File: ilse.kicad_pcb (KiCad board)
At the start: 2 copper layers, 80.9 x 128.5 mm, 89 parts, among them J1 OUT, J2 EURO RACK POWER, J3 CV Inputs, J4 1V/Oct, J5 Gate, J6 Cutoff, J7 Filter In, Q1 BC560, Q2 BC560, Q3 BC560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

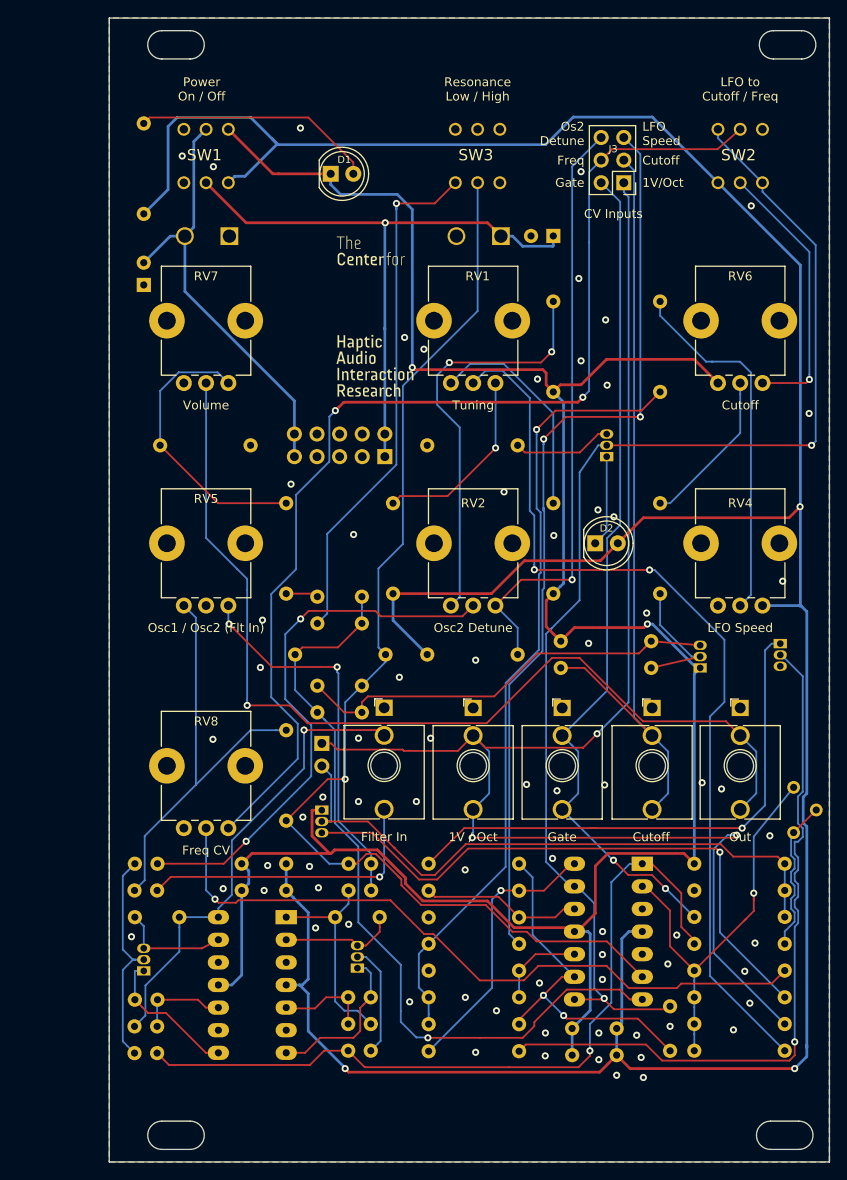
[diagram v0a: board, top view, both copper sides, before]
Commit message: removed power switch, added power protection diodes
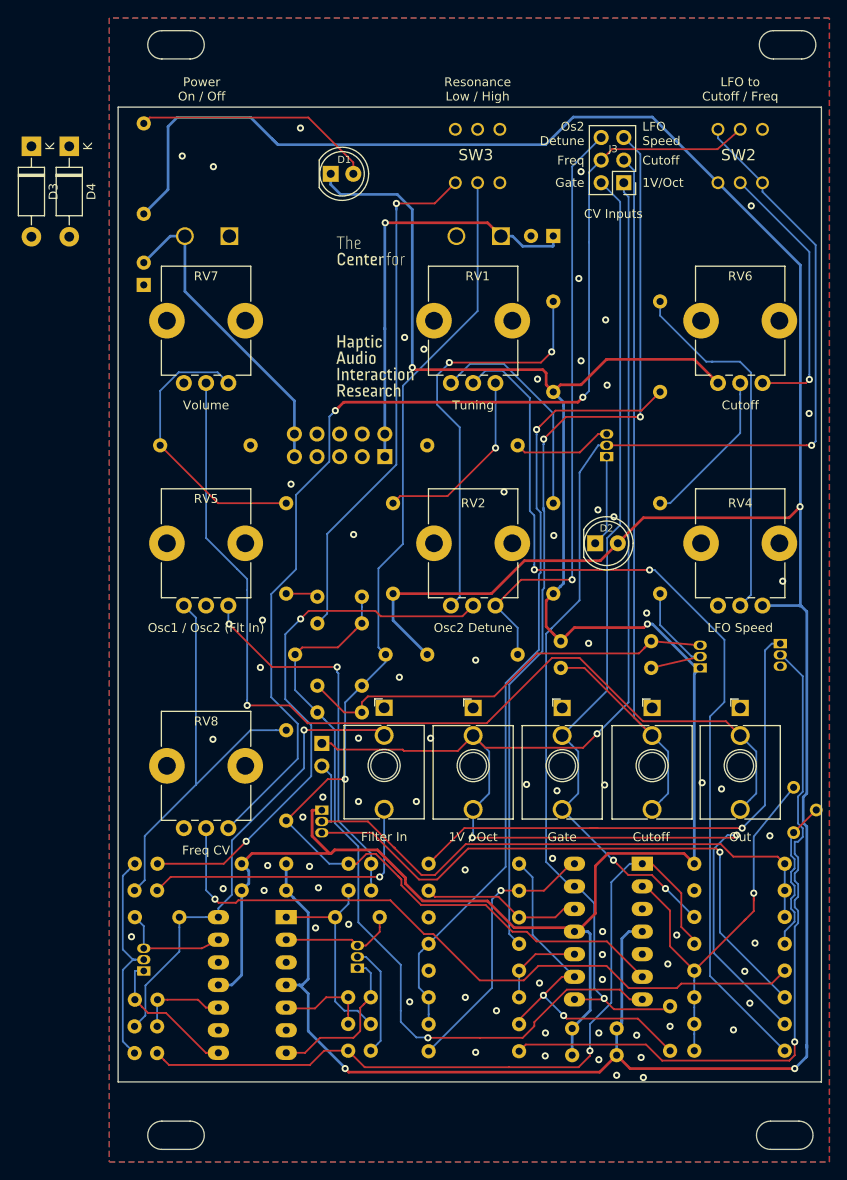
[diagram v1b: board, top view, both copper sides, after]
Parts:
- removed SW1: Power Switch, chair:PVA2
- added D3: 1N5819, Diode_THT:D_DO-41_SOD81_P10.16mm_Horizontal, F.Cu at (57.9, 52.4)
- added D4: 1N5819, Diode_THT:D_DO-41_SOD81_P10.16mm_Horizontal, F.Cu at (62.1, 52.4)
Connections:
- C12 pad 1: Net-(BT1-Pad1) -> VCC
- C13 pad 2: Net-(BT2-Pad2) -> VSS
- SW2 pad 4: Net-(SW2-Pad4) -> unconnected-(SW2-Pad4)
- SW3 pad 3: Net-(SW3-Pad3) -> unconnected-(SW3-Pad3)
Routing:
- net Net-(BT1-Pad1): track 69.6 -> 47.6 mm
- net VSS: track 271.1 -> 257.6 mm
- net Net-(BT2-Pad2): track 48.7 -> 35.7 mm
- net VCC: track 351.4 -> 344.1 mm
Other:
- board size 80.9 x 128.5 mm -> 79 x 109.5 mm
